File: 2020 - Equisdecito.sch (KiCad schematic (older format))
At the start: 36 parts, among them J1 VL53L0x_IZQ, J10 IMU, J11 Batería (-), J12 sharp2, J13 sharp2, J14 Arduino_Nano_Header, J15 sharp2, J16 MOTOR 1, J17 sharp2, J18 MOTOR 2, J19 AUX6, J2 VL53L0x_DER, J3 HC-05, J4 Pantalla Oled, J5 Batería (+), J6 sharp1, J7 tatami 1, J8 tatami 2, J9 Aux1, Q1 2N7002, SW1 Pulsador, U1 LM1117-SOT

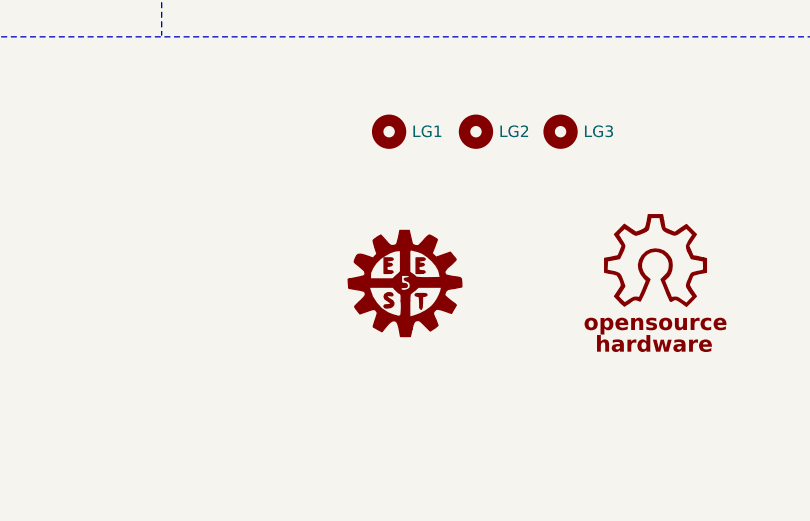
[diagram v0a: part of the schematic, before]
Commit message: MODIFICACIONES
se quito un logo en la capa bottom,se agrego descripción en el sch, y por ultimo se agrego revisión
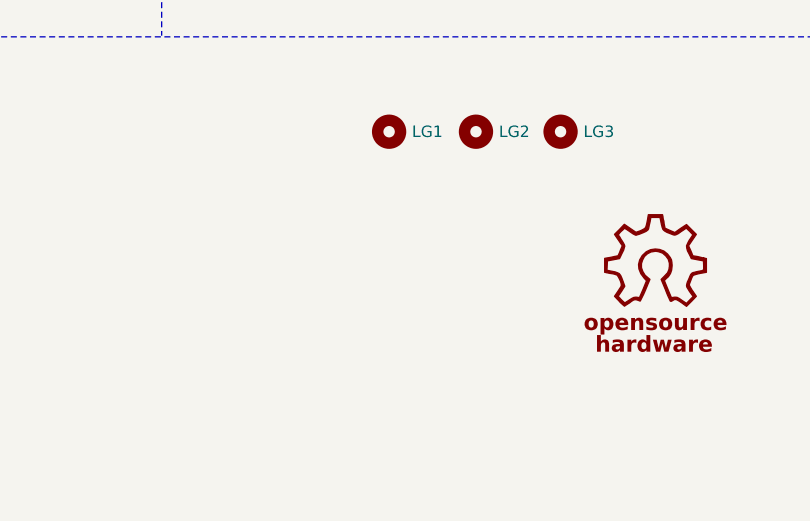
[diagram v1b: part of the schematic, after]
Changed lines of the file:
@@
 EESchema Schematic File Version 4
 LIBS:2020 - Equisdecito-cache
-EELAYER 29 0
+EELAYER 30 0
 EELAYER END
 $Descr A4 11693 8268
 encoding utf-8
 Sheet 1 1
-Title "Robot Mini Sumo"
-Date "2018-05-30"
+Title "Robot Sumo"
+Date "2021-01-07"
 Rev "1.0"
-Comp "E.E.S.T. N°5"
-Comment1 "Autor: Ing. Mariano Bustos"
-Comment2 "Club de Robótica"
+Comp "4 D E V"
+Comment1 "Autor: TEC. ZARATE ELIAS"
+Comment2 "4DEV ROBOTIC"
 Comment3 ""
 Comment4 ""
@@
 	1    0    0    -1
 $EndComp
-$Comp
-L EESTN5:LOGO_ROTULO #G1
-U 1 1 591C26A2
-P 9135 6830
-F 0 "#G1" H 9135 6608 60  0001 C CNN
-F 1 "LOGO_ROTULO" H 9135 7052 60  0001 C CNN
-F 2 "" H 9135 6830 60  0001 C CNN
-F 3 "" H 9135 6830 60  0001 C CNN
-	1    9135 6830
-	1    0    0    -1
-$EndComp
